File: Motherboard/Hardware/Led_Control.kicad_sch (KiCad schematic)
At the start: 22 parts, among them Q1 BCX51, Q10 BC848, Q2 BC848, Q3 BC848, Q4 BC848, Q5 BC848, Q6 BC848, Q7 BCX51, Q8 BC848, Q9 BC848

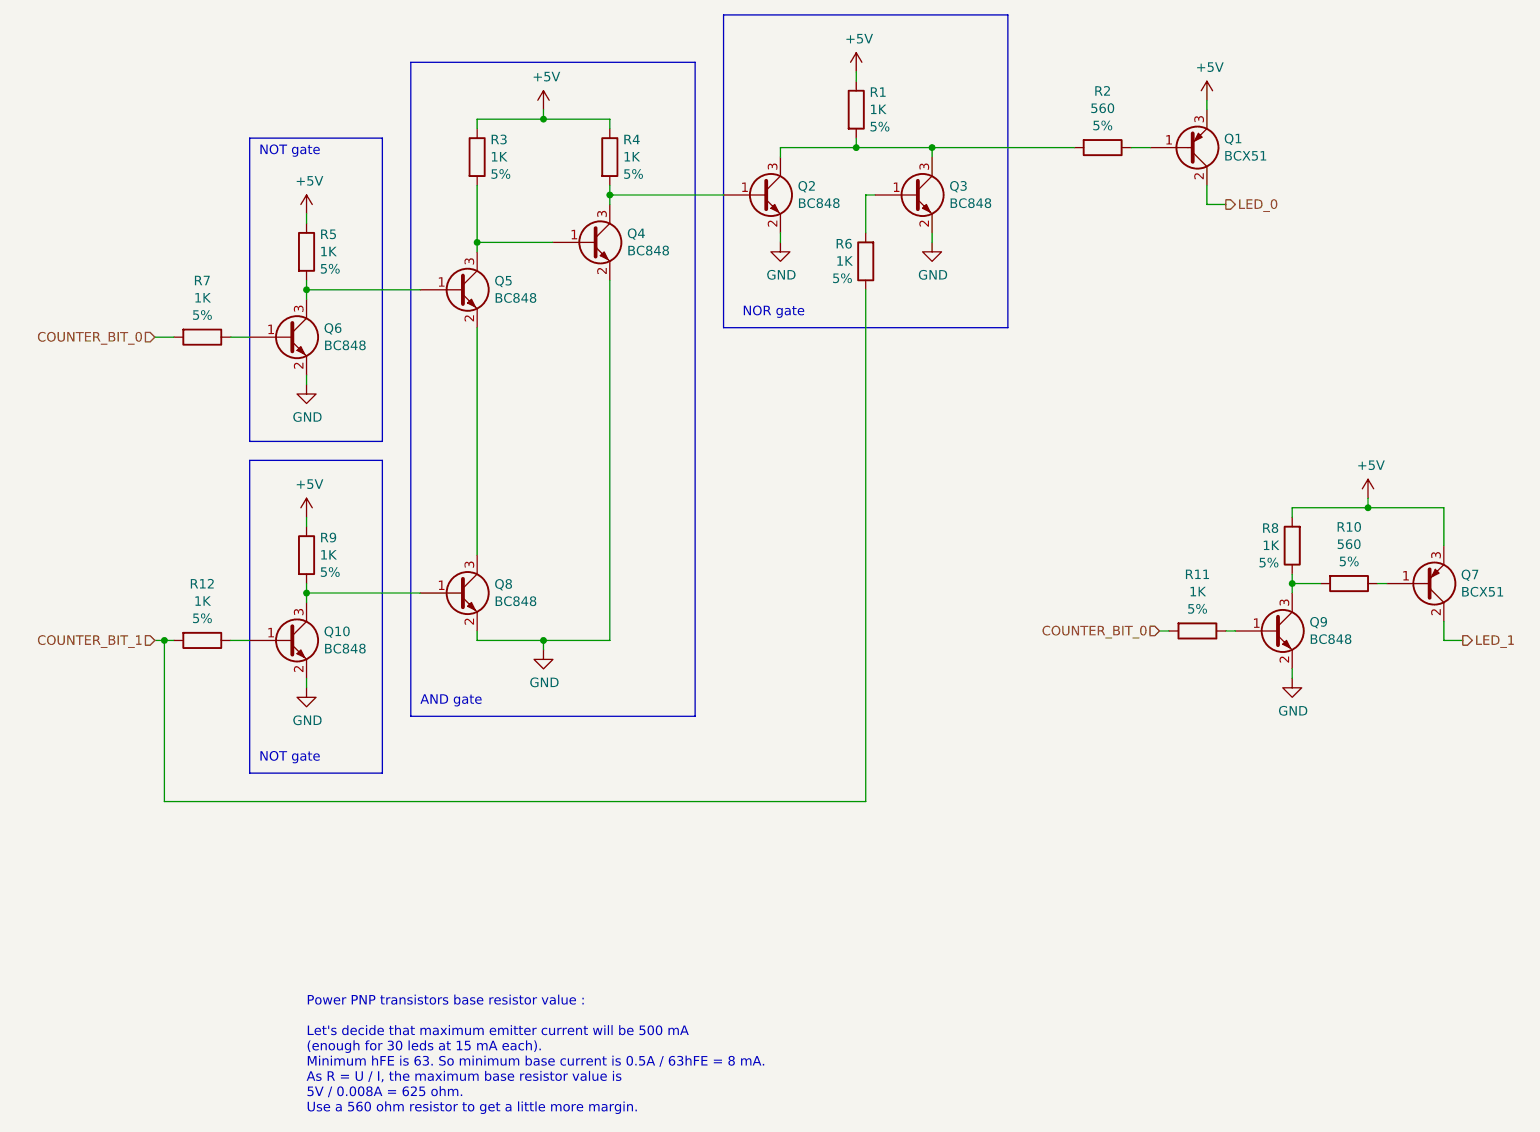
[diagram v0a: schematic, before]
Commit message: Updated the motherboard PCB to KiCad 7.
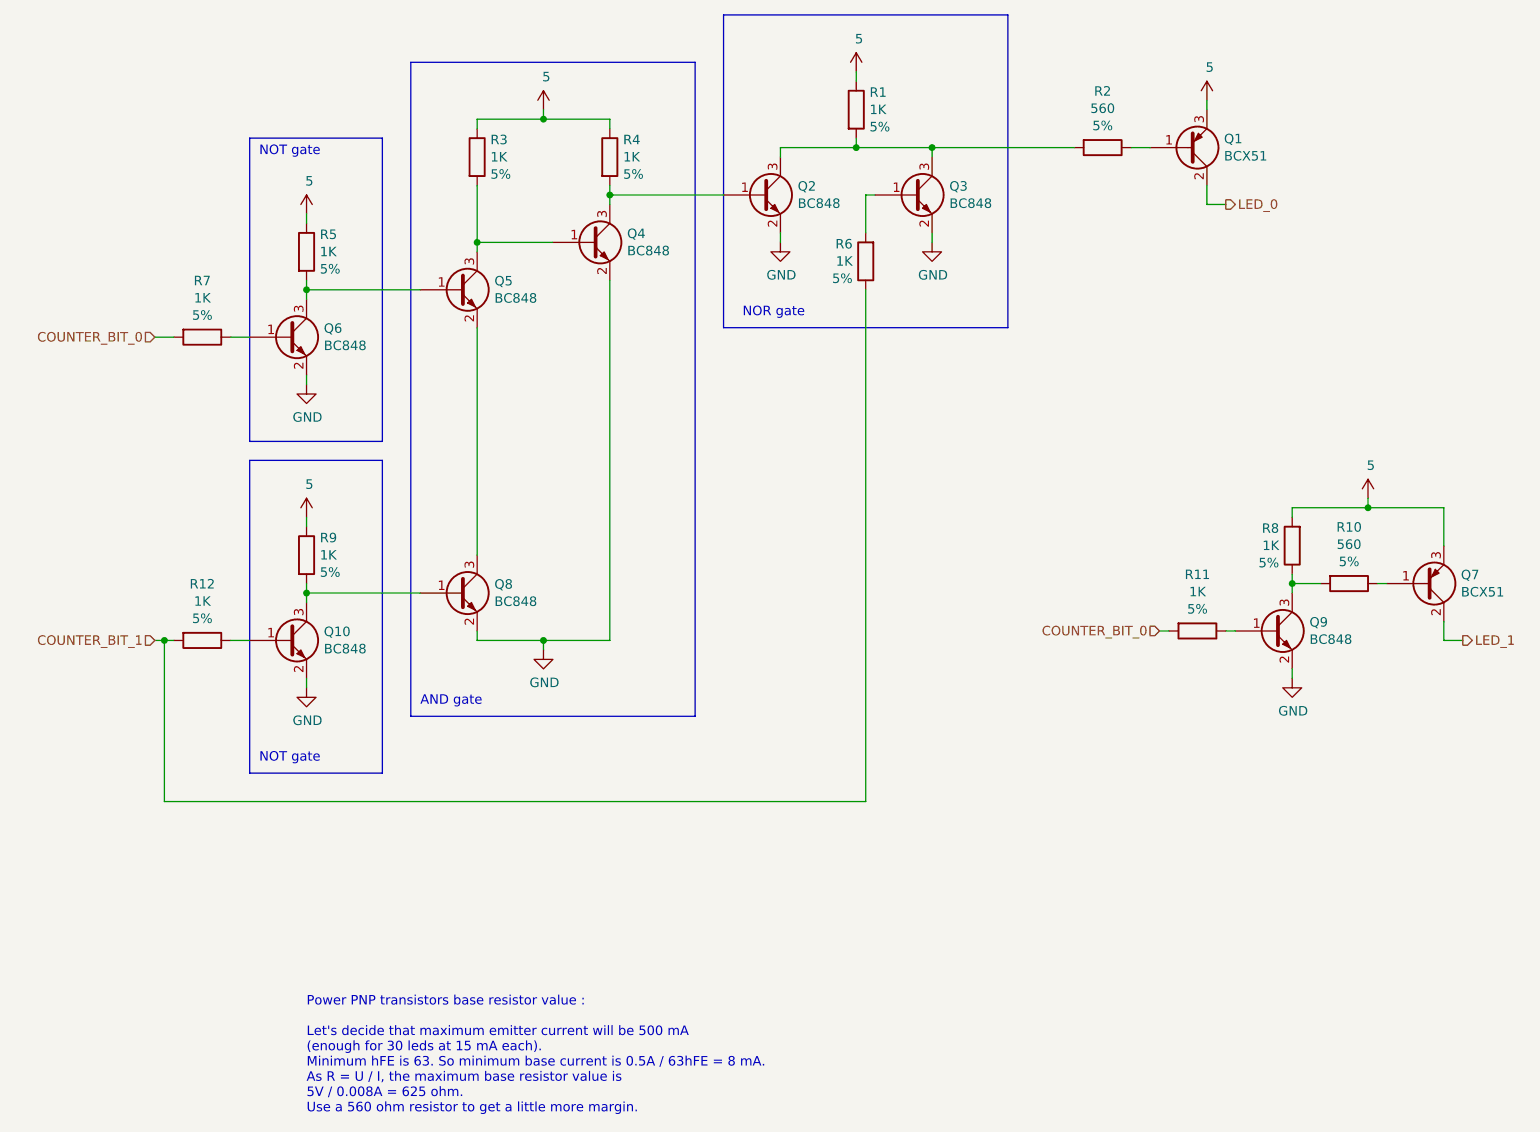
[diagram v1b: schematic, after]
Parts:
- Q1, Q7: Spice_Lib_File Spice_Simulation/BCX51.lib -> (none); Spice_Model BCX51 -> (none); Spice_Netlist_Enabled Y -> (none); Spice_Node_Sequence 3 1 2 -> (none); Spice_Primitive Q -> (none)
- Q10, Q2, Q3, Q4, Q5, Q6, Q8, Q9: Spice_Lib_File Spice_Simulation/BC848.lib -> (none); Spice_Model BC848 -> (none); Spice_Netlist_Enabled Y -> (none); Spice_Node_Sequence 3 1 2 -> (none); Spice_Primitive Q -> (none)
- R1, R10, R11, R12, R2, R3, R4, R5, R6, R7, R8, R9: Spice_Model 1k -> (none); Spice_Netlist_Enabled Y -> (none); Spice_Primitive R -> (none)
